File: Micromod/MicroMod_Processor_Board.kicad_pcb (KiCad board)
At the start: 4 copper layers, 22 x 22 mm, 4 parts, among them J1 MICROMOD-2222

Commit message: progress so far
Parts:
- added C1: 1u, Capacitor_SMD:C_0603_1608Metric_Pad1.08x0.95mm_HandSolder, F.Cu at (147.8, 91.6)
- added C10: 2.2uF, Capacitor_SMD:C_0603_1608Metric_Pad1.08x0.95mm_HandSolder, F.Cu at (152.8, 96.2)
- added C11: 100n, Capacitor_SMD:C_0603_1608Metric_Pad1.08x0.95mm_HandSolder, B.Cu at (145.3, 109.3)
- added C12: 100n, Capacitor_SMD:C_0603_1608Metric_Pad1.08x0.95mm_HandSolder, F.Cu at (96.3, 96.2)
- added C13: 100n, Capacitor_SMD:C_0603_1608Metric_Pad1.08x0.95mm_HandSolder, F.Cu at (96.3, 98.7)
- added C14: 100n, Capacitor_SMD:C_0603_1608Metric_Pad1.08x0.95mm_HandSolder, F.Cu at (96.3, 101.2)
- added C15: 100n, Capacitor_SMD:C_0603_1608Metric_Pad1.08x0.95mm_HandSolder, F.Cu at (96.3, 103.7)
- added C16: 100n, Capacitor_SMD:C_0603_1608Metric_Pad1.08x0.95mm_HandSolder, B.Cu at (148.8, 109.2)
- added C17: 100n, Capacitor_SMD:C_0603_1608Metric_Pad1.08x0.95mm_HandSolder, F.Cu at (131.6, 107.5)
- added C18: 2.2uF, Capacitor_SMD:C_0603_1608Metric_Pad1.08x0.95mm_HandSolder, F.Cu at (131.6, 106.0)
- added C2: 6.8pF, Capacitor_SMD:C_0603_1608Metric_Pad1.08x0.95mm_HandSolder, F.Cu at (144.7, 89.7)
- added C3: 6.8pF, Capacitor_SMD:C_0603_1608Metric_Pad1.08x0.95mm_HandSolder, F.Cu at (141.4, 89.7)
- added C4: 100n, Capacitor_SMD:C_0603_1608Metric_Pad1.08x0.95mm_HandSolder, F.Cu at (149.8, 80.2)
- added C5: 4.7uF, Capacitor_SMD:C_0603_1608Metric_Pad1.08x0.95mm_HandSolder, F.Cu at (92.0, 98.7)
- added C6: 10uF, Capacitor_SMD:C_0603_1608Metric_Pad1.08x0.95mm_HandSolder, F.Cu at (92.0, 101.2)
- added C7: 100n, Capacitor_SMD:C_0603_1608Metric_Pad1.08x0.95mm_HandSolder, F.Cu at (92.0, 103.7)
- added C8: 1uF, Capacitor_SMD:C_0603_1608Metric_Pad1.08x0.95mm_HandSolder, F.Cu at (92.0, 106.2)
- added C9: 100n, Capacitor_SMD:C_0603_1608Metric_Pad1.08x0.95mm_HandSolder, F.Cu at (138.0, 91.0)
- added F1: 0.2A, Resistor_SMD:R_0805_2012Metric_Pad1.20x1.40mm_HandSolder, B.Cu at (156.7, 109.0)
- added J2: Micro_SD_Card, Connector_Card:microSD_HC_Wuerth_693072010801, B.Cu at (143.8, 100.0)
- added J3: WiFi_BT_CONN_2, Library:CONN20_DF40HC-25-20DS_HIR, F.Cu at (130.0, 100.1)
- added J4: WiFi_BT_CONN_1, Library:CONN20_DF40HC-25-20DS_HIR, F.Cu at (155.5, 100.6)
- added J5: TRACE, Connector_PinHeader_1.27mm:PinHeader_2x10_P1.27mm_Vertical_SMD, F.Cu at (141.9, 82.0)
- added Q1: FDN340P, Package_TO_SOT_SMD:SOT-23, F.Cu at (157.4, 94.9)
- added R1: R, Resistor_SMD:R_0603_1608Metric_Pad0.98x0.95mm_HandSolder, F.Cu at (100.7, 93.7)
- added R2: 100k, Resistor_SMD:R_0603_1608Metric_Pad0.98x0.95mm_HandSolder, F.Cu at (100.7, 96.2)
- added R3: DNP, Resistor_SMD:R_0603_1608Metric_Pad0.98x0.95mm_HandSolder, B.Cu at (132.3, 92.6)
- added U1: STM32H562VGTx, Package_QFP:LQFP-100_14x14mm_P0.5mm, F.Cu at (142.3, 101.4)
- added Y1: ABS07AIG-32.768KHZ, Resistor_SMD:R_1206_3216Metric_Pad1.30x1.75mm_HandSolder, F.Cu at (143.6, 91.5)
- moved LOGO3 23.4 mm to (176.5, 110.2)
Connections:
- net 3.3V renamed Net-(F1-Pad2)
- net Net-(J1-Pad4) renamed /3.3V_EN
- net V_USB renamed /V_USB
- J1 pad 10: /14-D0 -> /D0
- J1 pad 11: /0-~{BOOT} -> /~{BOOT}
- J1 pad 12: /21-SDA -> /I2C_SDA
- J1 pad 13: Net-(J1-Pad13) -> /UART_RTS1
- J1 pad 14: /22-SCL -> /I2C_SCL
- J1 pad 15: Net-(J1-Pad15) -> /UART_CTS1
- J1 pad 16: /4-I2C_~{INT} -> /I2C_~{INT}
- J1 pad 17: /17-G3/TX1/AUD_OUT -> /UART_TX1
- J1 pad 18: /27-D1 -> /D1-CAM_TRIG
- J1 pad 19: /16-G4/RX1/AUD_IN -> /UART_RX1
- J1 pad 20: Net-(J1-Pad20) -> /UART_RX2
- J1 pad 21: Net-(J1-Pad21) -> /SWDCK
- J1 pad 22: Net-(J1-Pad22) -> /UART_TX2
- J1 pad 23: Net-(J1-Pad23) -> /SWDIO
- J1 pad 3: /D+ -> /USB_D+
- J1 pad 32: /13-PWM0 -> /PWM0
- J1 pad 34: /34-A0 -> /A0
- J1 pad 35: Net-(J1-Pad35) -> unconnected-(J1-USBHOST_D+-Pad35)
- J1 pad 37: Net-(J1-Pad37) -> unconnected-(J1-USBHOST_D--Pad37)
- J1 pad 38: /35-A1 -> /A1
- J1 pad 40: /15-G0 -> /G0
- J1 pad 41: Net-(J1-Pad41) -> /CAN-RX
- J1 pad 42: /25-G1/AUD_LRCLK/SCL1 -> /G1
- J1 pad 43: Net-(J1-Pad43) -> /CAN-TX
- J1 pad 44: /26-G2/AUD_BCLK/SDA1 -> /G2
- J1 pad 46: /17-G3/TX1/AUD_OUT -> /G3
- J1 pad 47: /12-PWM1 -> /PWM1
- J1 pad 48: /16-G4/RX1/AUD_IN -> /G4
- J1 pad 49: /39-BATT/3 -> /BATT_VIN
- J1 pad 5: /D- -> /USB_D-
- J1 pad 50: /26-G2/AUD_BCLK/SDA1 -> /AUD_BCLK
- J1 pad 51: /26-G2/AUD_BCLK/SDA1 -> /I2C_SDA1
- J1 pad 52: /25-G1/AUD_LRCLK/SCL1 -> /AUD_LRCLK
- J1 pad 53: /25-G1/AUD_LRCLK/SCL1 -> /I2C_SCL1
- J1 pad 54: /16-G4/RX1/AUD_IN -> /AUD_IN-CAM_PCLK
- J1 pad 55: /5-~{CS} -> /~{SPI_CS}
- J1 pad 56: /17-G3/TX1/AUD_OUT -> /AUD_OUT-CAM_MCLK
- J1 pad 57: /18-SCK -> /SPI_SCK
- J1 pad 58: Net-(J1-Pad58) -> /AUD_MCLK
- J1 pad 59: /23-COPI -> /SPI_MOSI
- J1 pad 60: Net-(J1-Pad60) -> /SPI_SCK1
- J1 pad 61: /19-CIPO -> /SPI_MISO
- J1 pad 62: Net-(J1-Pad62) -> /SPI_COPI1
- J1 pad 63: Net-(J1-Pad63) -> unconnected-(J1-G10/ADC_D+/CAM_VSYNC-Pad63)
- J1 pad 64: Net-(J1-Pad64) -> /SPI_CIPO1
- J1 pad 65: Net-(J1-Pad65) -> unconnected-(J1-G9/ADC_D-/CAM_HSYNC-Pad65)
- J1 pad 66: Net-(J1-Pad66) -> unconnected-(J1-SDIO_DATA1-Pad66)
- J1 pad 67: Net-(J1-Pad67) -> unconnected-(J1-G8-Pad67)
- J1 pad 68: Net-(J1-Pad68) -> unconnected-(J1-SDIO_DATA2-Pad68)
- J1 pad 69: Net-(J1-Pad69) -> /G7
- J1 pad 70: Net-(J1-Pad70) -> /~{SPI_CS1}
- J1 pad 71: /33-G6/RTC -> /G6
- J1 pad 72: Net-(J1-Pad72) -> /VBAT
- J1 pad 73: /32-G5/RTC -> /G5
- J1 pad 8: Net-(J1-Pad8) -> /G11-SWO
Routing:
- net +3.3V: track 0.00 -> 65.9 mm, vias 0 -> 9
- net GND: track 0.00 -> 50.0 mm, vias 0 -> 8
- net /G5: track 0.00 -> 35.9 mm, vias 0 -> 2
- net /G7: track 0.00 -> 35.8 mm, vias 0 -> 2
- net /UART_TX1: track 0.00 -> 34.8 mm, vias 0 -> 2
- net /VBAT: track 0.00 -> 27.9 mm, vias 0 -> 2
- net /A0: track 0.00 -> 26.3 mm, vias 0 -> 1
- net /A1: track 0.00 -> 26.2 mm, vias 0 -> 1
- net /BT_PCM_CLK: track 0.00 -> 25.1 mm
- net Net-(F1-Pad2): track 0.00 -> 24.1 mm, vias 0 -> 2
- net /~{BOOT}: track 0.00 -> 23.8 mm, vias 0 -> 2
- net /G6: track 0.00 -> 23.5 mm, vias 0 -> 2
- net /I2C_SDA1: track 0.00 -> 23.4 mm, vias 0 -> 2
- net /BT_REG_ON: track 0.00 -> 23.0 mm, vias 0 -> 2
- net /AUD_LRCLK: track 0.00 -> 23.0 mm, vias 0 -> 1
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- added copper zone on B.Cu, net GND
- added copper zone on F.Cu, net GND
- added copper zone on In1.Cu, net GND
- added copper zone on In2.Cu, net GND
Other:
- board size 22 x 22 mm -> 32.5 x 37.5 mm

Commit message: almost done routing
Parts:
- C10, C13: moved to B.Cu
- LOGO3: moved to F.Cu
- moved C5 66.1 mm to (157.4, 108.2)
- moved C6 65.7 mm to (157.5, 106.7)
- moved C8 63.1 mm to (155.0, 109.0), turned to 90 degrees
- moved C12 61.9 mm to (157.6, 105.1), turned to 180 degrees
- moved R1 57.9 mm to (158.6, 95.3), turned to -90 degrees
- moved C13 57.4 mm to (153.6, 95.9), turned to 180 degrees
- moved R2 51.5 mm to (152.2, 97.1), turned to 90 degrees
- moved LOGO3 47.7 mm to (128.8, 108.4), turned to 0 degrees
- moved C7 45.7 mm to (135.9, 91.0), turned to -90 degrees
- moved C14 42.4 mm to (137.5, 91.0), turned to -90 degrees
- moved C15 37.2 mm to (132.3, 94.2)
- moved R3 21.8 mm to (152.6, 100.6)
- moved Q1 1.58 mm to (155.9, 95.3), turned to 180 degrees
- moved C10 1.42 mm to (153.6, 97.4)
- moved C9 1.04 mm to (139.0, 91.1)
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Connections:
- J1 pad 32: /PWM0 -> unconnected-(J1-PWM0-Pad32)
- J1 pad 47: /PWM1 -> unconnected-(J1-PWM1-Pad47)
- J1 pad 48: /G4 -> unconnected-(J1-G4/BUS4-Pad48)
- J5 pad 8: /G6 -> unconnected-(J5-Pin_8-Pad8)
- U1 pad 18: /G3 -> /PWM0
- U1 pad 24: /D1-CAM_TRIG -> /BT_REG_ON
- U1 pad 46: /G2 -> /BT_DEV_WAKE
- U1 pad 51: /~{SPI_CS} -> /WL_REG_ON
- U1 pad 57: /G4 -> /PWM1
- U1 pad 60: /BT_REG_ON -> /G5
- U1 pad 61: /WL_REG_ON -> /G6
- U1 pad 62: /BT_DEV_WAKE -> /G7
- U1 pad 67: /PWM1 -> /~{SPI_CS}
- U1 pad 68: /WL_GPIO_0_HOST_WAKE -> /G3
- U1 pad 69: /PWM0 -> /G2
- U1 pad 77: /G6 -> /G1
- U1 pad 84: /G7 -> /WL_GPIO_0_HOST_WAKE
- U1 pad 85: /G5 -> /D1-CAM_TRIG
- U1 pad 97: /G1 -> unconnected-(U1-PE0-Pad97)
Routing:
- net +3.3V: track 65.9 -> 147.2 mm, vias 9 -> 17
- net GND: track 50.0 -> 115.7 mm, vias 8 -> 23
- net /~{RESET}: track 0.00 -> 45.8 mm, vias 0 -> 1
- net /UART_CTS1: track 0.00 -> 42.3 mm, vias 0 -> 4
- net /UART_RTS1: track 0.00 -> 41.6 mm, vias 0 -> 4
- net /D0: track 0.00 -> 37.0 mm, vias 0 -> 1
- net /UART_RX1: track 1.95 -> 36.7 mm, vias 1 -> 4
- net /G5: track 35.9 -> 5.21 mm, vias 2 -> 0
- net /G7: track 35.8 -> 5.20 mm, vias 2 -> 0
- net /SWDCK: track 8.55 -> 38.1 mm
- net /G11-SWO: track 17.0 -> 44.5 mm
- net /SWDIO: track 11.5 -> 36.9 mm
- net /SPI_MISO: track 0.00 -> 25.4 mm, vias 0 -> 2
- net /SPI_MOSI: track 0.00 -> 24.8 mm, vias 0 -> 2
- net /UART_RX2: track 0.00 -> 22.8 mm, vias 0 -> 1
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
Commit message: almost ready for review
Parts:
- Q1, R1: moved to B.Cu
- moved LOGO3 16.9 mm to (130.8, 91.6)
- moved J3 3.27 mm to (131.0, 103.2)
- moved R1 2.66 mm to (157.9, 97.9), turned to 90 degrees
- moved C17 1.91 mm to (130.5, 109.1)
- moved C18 1.89 mm to (130.5, 107.6)
- moved Q1 1.66 mm to (157.3, 94.5), turned to 0 degrees
- moved C1 0.99 mm to (148.8, 91.3)
- moved C15 0.38 mm to (132.7, 94.2)
- moved Y1 0.22 mm to (143.4, 91.5)
- moved C9 0.07 mm to (139.0, 91.0)
- turned C16 to 180 degrees
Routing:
- net GND: track 115.7 -> 150.1 mm, vias 23 -> 28
- net +3.3V: track 147.2 -> 156.9 mm, vias 17 -> 15
- net /~{RESET}: track 45.8 -> 51.1 mm
- net Net-(C18-Pad1): track 2.27 -> 7.13 mm
- net /BOOT0: track 6.53 -> 9.92 mm, vias 0 -> 1
- net /A1: track 25.2 -> 28.6 mm
- net Net-(F1-Pad2): track 24.2 -> 27.6 mm
- net /BT_UART_RX: track 5.59 -> 2.44 mm
- net /BT_UART_RTS: track 5.61 -> 2.48 mm
- net /BT_UART_TX: track 5.44 -> 2.40 mm
- net /BT_PCM_OUT: track 10.6 -> 7.67 mm
- net /UART_RX2: track 22.8 -> 20.1 mm
- net /BT_HOST_WAKE: track 13.4 -> 16.0 mm
- net /BT_UART_CTS: track 5.16 -> 2.61 mm
- net /WL_REG_ON: track 16.5 -> 14.2 mm
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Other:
- board size 32.5 x 37.5 mm -> 31.4 x 37.5 mm

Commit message: done
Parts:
- added D1: LED, LED_SMD:LED_0603_1608Metric_Pad1.05x0.95mm_HandSolder, F.Cu at (157.3, 93.7)
- added R4: 470, Resistor_SMD:R_0603_1608Metric_Pad0.98x0.95mm_HandSolder, F.Cu at (157.2, 96.0)
- added R5: 1k, Resistor_SMD:R_0603_1608Metric_Pad0.98x0.95mm_HandSolder, B.Cu at (154.7, 109.3)
- moved R3 0.47 mm to (153.1, 100.4)
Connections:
- J1 pad 4: /3.3V_EN -> unconnected-(J1-3.3V_EN-Pad4)
- J1 pad 9: /V_USB -> Net-(J1-USB_VIN)
- J4 pad 5: unconnected-(J4-Pin_5-Pad5) -> GND
- J4 pad 7: unconnected-(J4-Pin_7-Pad7) -> GND
- U1 pad 18: /PWM0 -> /USB_VIN
- U1 pad 57: /PWM1 -> unconnected-(U1-PD10-Pad57)
- U1 pad 97: unconnected-(U1-PE0-Pad97) -> Net-(U1-PE0)
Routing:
- net GND: track 150.1 -> 366.9 mm, vias 28 -> 88
- net /USB_VIN: track 0.00 -> 28.7 mm, vias 0 -> 1
- net Net-(U1-PE0): track 0.00 -> 9.14 mm
- net /G11-SWO: track 44.8 -> 41.4 mm
- net /TRACE_D0: track 19.3 -> 16.1 mm
- net /A1: track 28.6 -> 25.7 mm
- net Net-(J1-USB_VIN): track 0.00 -> 2.81 mm, vias 0 -> 1
- net /SPI_MISO: track 25.2 -> 22.4 mm
- net /G0: track 17.0 -> 14.5 mm
- net /VBAT: track 35.5 -> 33.5 mm
- net /TRACE_D1: track 16.0 -> 17.9 mm
- net Net-(D1-A): track 0.00 -> 1.82 mm
- net /BT_PCM_CLK: track 22.0 -> 20.5 mm
- net /SD_DAT0: track 16.5 -> 15.1 mm
- net /D0: track 37.3 -> 38.6 mm
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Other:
- board text added: "STAT"

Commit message: add some changes, make ibom from both pcbs
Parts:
- R1: value R -> 100k
- U1: value STM32H562VGTx -> STM32H563VGTx
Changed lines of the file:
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@@
 			)
 		)
-		(property "LCSC" "C25803"
-			(at 0 0 0)
-			(layer "F.SilkS")
-			(hide yes)
-			(effects
-				(font
-					(size 1.27 1.27)
-					(thickness 0.15)
-				)
-			)
-		)
 		(property ki_fp_filters "R_*")
 		(sheetname "/")
@@
 			)
 		)
-		(property "LCSC" "C23630"
-			(at 0 0 0)
-			(layer "F.SilkS")
-			(hide yes)
-			(effects
-				(font
-					(size 1.27 1.27)
-					(thickness 0.15)
-				)
-			)
-		)
 		(property ki_fp_filters "C_*")
 		(sheetname "/")
@@
 			)
 		)
-		(property "LCSC" "C2286"
-			(at 0 0 0)
-			(layer "F.SilkS")
-			(hide yes)
-			(effects
-				(font
-					(size 1.27 1.27)
-					(thickness 0.15)
-				)
-			)
-		)
 		(property ki_fp_filters "LED* LED_SMD:* LED_THT:*")
 		(sheetname "/")
@@
 			)
 		)
-		(property "LCSC" "C23179"
-			(at 0 0 0)
-			(layer "F.SilkS")
-			(hide yes)
-			(effects
-				(font
-					(size 1.27 1.27)
-					(thickness 0.15)
-				)
-			)
-		)
 		(property ki_fp_filters "R_*")
 		(sheetname "/")
@@
 			)
 		)
-		(property "LCSC" "C1985604"
-			(at 0 0 0)
-			(layer "F.SilkS")
-			(hide yes)
-			(effects
-				(font
-					(size 1.27 1.27)
-					(thickness 0.15)
-				)
-			)
-		)
 		(property ki_fp_filters "Crystal*")
 		(sheetname "/")
@@
 			)
 		)
-		(property "Value" "STM32H562VGTx"
+		(property "Value" "STM32H563VGTx"
 			(at 0 9.43 90)
 			(layer "F.Fab")
@@
 			)
 		)
-		(property "LCSC" "C22452133"
-			(at 0 0 0)
-			(layer "F.SilkS")
-			(hide yes)
-			(effects
-				(font
-					(size 1.27 1.27)
-					(thickness 0.15)
-				)
-			)
-		)
 		(property ki_fp_filters "LQFP*14x14mm*P0.5mm*")
 		(sheetname "/")
@@
 			)
 		)
-		(property "LCSC" "C3032587"
-			(at 0 0 0)
-			(layer "F.SilkS")
-			(hide yes)
-			(effects
-				(font
-					(size 1.27 1.27)
-					(thickness 0.15)
-				)
-			)
-		)
 		(property ki_fp_filters "Connector*:*_2x??_*")
 		(sheetname "/")
@@
 		(sheetname "/")
 		(sheetfile "MicroMod_Processor_Board.kicad_sch")
-		(attr smd exclude_from_pos_files exclude_from_bom)
+		(attr smd exclude_from_pos_files)
 		(fp_line
 			(start -0.146267 0.51)
@@
 		(sheetname "/")
 		(sheetfile "MicroMod_Processor_Board.kicad_sch")
-		(attr smd exclude_from_pos_files exclude_from_bom)
+		(attr smd exclude_from_pos_files)
 		(fp_line
 			(start -0.227064 -0.735)
@@
 			)
 		)
-		(property "Value" "R"
+		(property "Value" "100k"
 			(at 0 -1.43 90)
 			(layer "B.Fab")
@@
 		(sheetname "/")
 		(sheetfile "MicroMod_Processor_Board.kicad_sch")
-		(attr smd exclude_from_pos_files exclude_from_bom)
+		(attr smd exclude_from_pos_files)
 		(fp_line
 			(start -0.254724 -0.5225)
@@
 		(sheetname "/")
 		(sheetfile "MicroMod_Processor_Board.kicad_sch")
-		(attr smd exclude_from_pos_files exclude_from_bom)
+		(attr smd exclude_from_pos_files)
 		(fp_line
 			(start -0.146267 -0.51)
@@
 		(sheetname "/")
 		(sheetfile "MicroMod_Processor_Board.kicad_sch")
-		(attr smd exclude_from_pos_files exclude_from_bom)
+		(attr smd exclude_from_pos_files)
 		(fp_line
 			(start 0 -1.56)
@@
 		(sheetname "/")
 		(sheetfile "MicroMod_Processor_Board.kicad_sch")
-		(attr smd exclude_from_pos_files exclude_from_bom)
+		(attr smd exclude_from_pos_files)
 		(fp_line
 			(start -0.146267 -0.51)
@@
 		(sheetname "/")
 		(sheetfile "MicroMod_Processor_Board.kicad_sch")
-		(attr smd exclude_from_pos_files exclude_from_bom)
+		(attr smd exclude_from_pos_files)
 		(fp_line
 			(start -0.254724 -0.5225)
@@
 		(sheetname "/")
 		(sheetfile "MicroMod_Processor_Board.kicad_sch")
-		(attr smd exclude_from_pos_files exclude_from_bom)
+		(attr smd exclude_from_pos_files)
 		(fp_line
 			(start 6.91 5.81)
@@
 		(sheetname "/")
 		(sheetfile "MicroMod_Processor_Board.kicad_sch")
-		(attr smd exclude_from_pos_files exclude_from_bom)
+		(attr smd exclude_from_pos_files)
 		(fp_line
 			(start -0.254724 0.5225)
@@
 		(sheetname "/")
 		(sheetfile "MicroMod_Processor_Board.kicad_sch")
-		(attr smd exclude_from_pos_files exclude_from_bom)
+		(attr smd exclude_from_pos_files)
 		(fp_line
 			(start -0.146267 0.51)

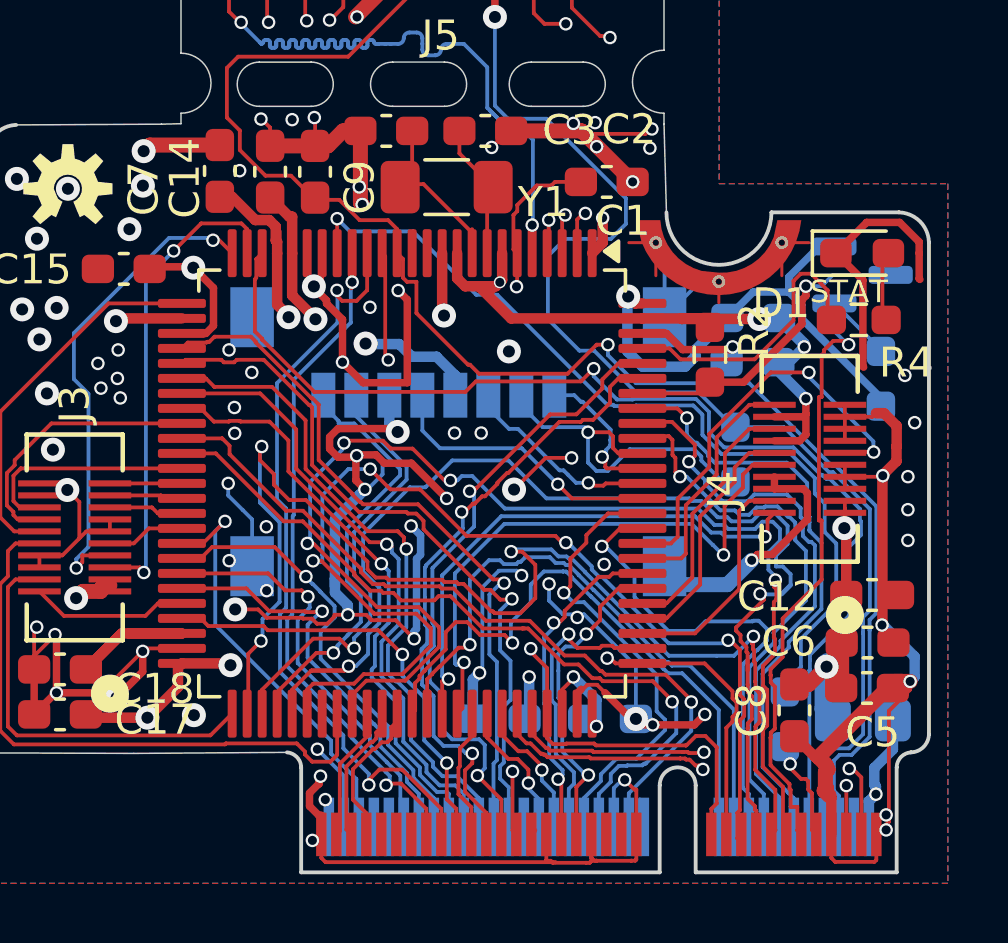
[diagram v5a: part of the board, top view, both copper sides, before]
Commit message: fix the rts/cts line being swapped and missing led0 connection (PWM0)
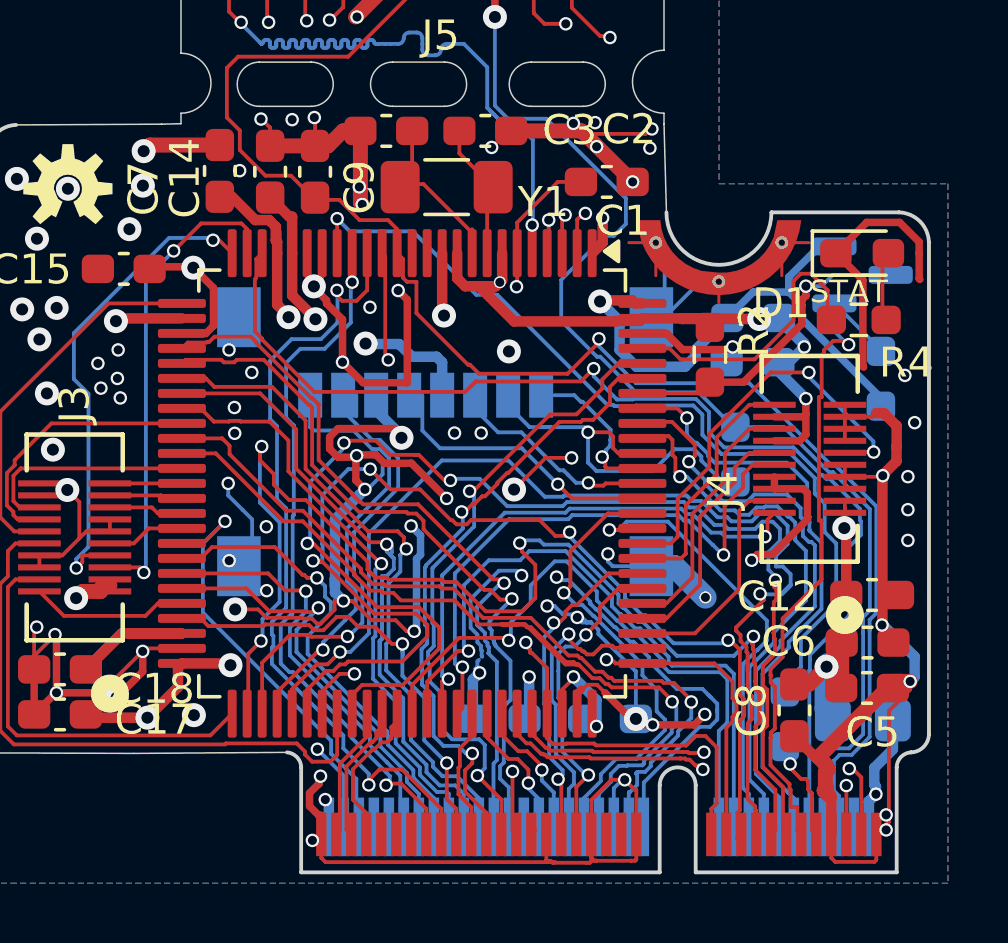
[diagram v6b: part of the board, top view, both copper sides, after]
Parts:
- moved J2 0.44 mm to (143.4, 100.0)
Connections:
- J1 pad 32: unconnected-(J1-PWM0-Pad32) -> /PWM0
- U1 pad 57: unconnected-(U1-PD10-Pad57) -> /PWM0
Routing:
- net /PWM0: track 0.00 -> 26.3 mm, vias 0 -> 2
- net GND: track 366.9 -> 373.1 mm, vias 88 -> 89
- net /AUD_OUT-CAM_MCLK: track 21.1 -> 24.7 mm
- net /A1: track 25.7 -> 29.3 mm
- net +3.3V: track 158.2 -> 161.5 mm
- net /UART_TX1: track 38.9 -> 36.7 mm
- net /G11-SWO: track 41.4 -> 40.1 mm
- net /UART_RX2: track 20.5 -> 21.7 mm
- net /SPI_MOSI: track 25.6 -> 26.6 mm
- net unconnected-(J1-PWM0-Pad32): track 0.98 -> 0.00 mm
- net /SPI_MISO: track 22.4 -> 23.4 mm
- net /SPI_SCK: track 14.6 -> 15.6 mm
- net unconnected-(U1-PD10-Pad57): track 0.62 -> 0.00 mm
